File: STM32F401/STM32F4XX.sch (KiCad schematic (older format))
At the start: 34 parts, among them J1 DEBUG UART, J2 Conn_02x16_Counter_Clockwise, J3 USB_B_Mini, J4 Conn_02x16_Counter_Clockwise, J5 JTAG SWDIO SWCLK, SW1 ~RESET, U1 STM32F401RCT6, U2 LM1117-3.3, Y1 8MHz

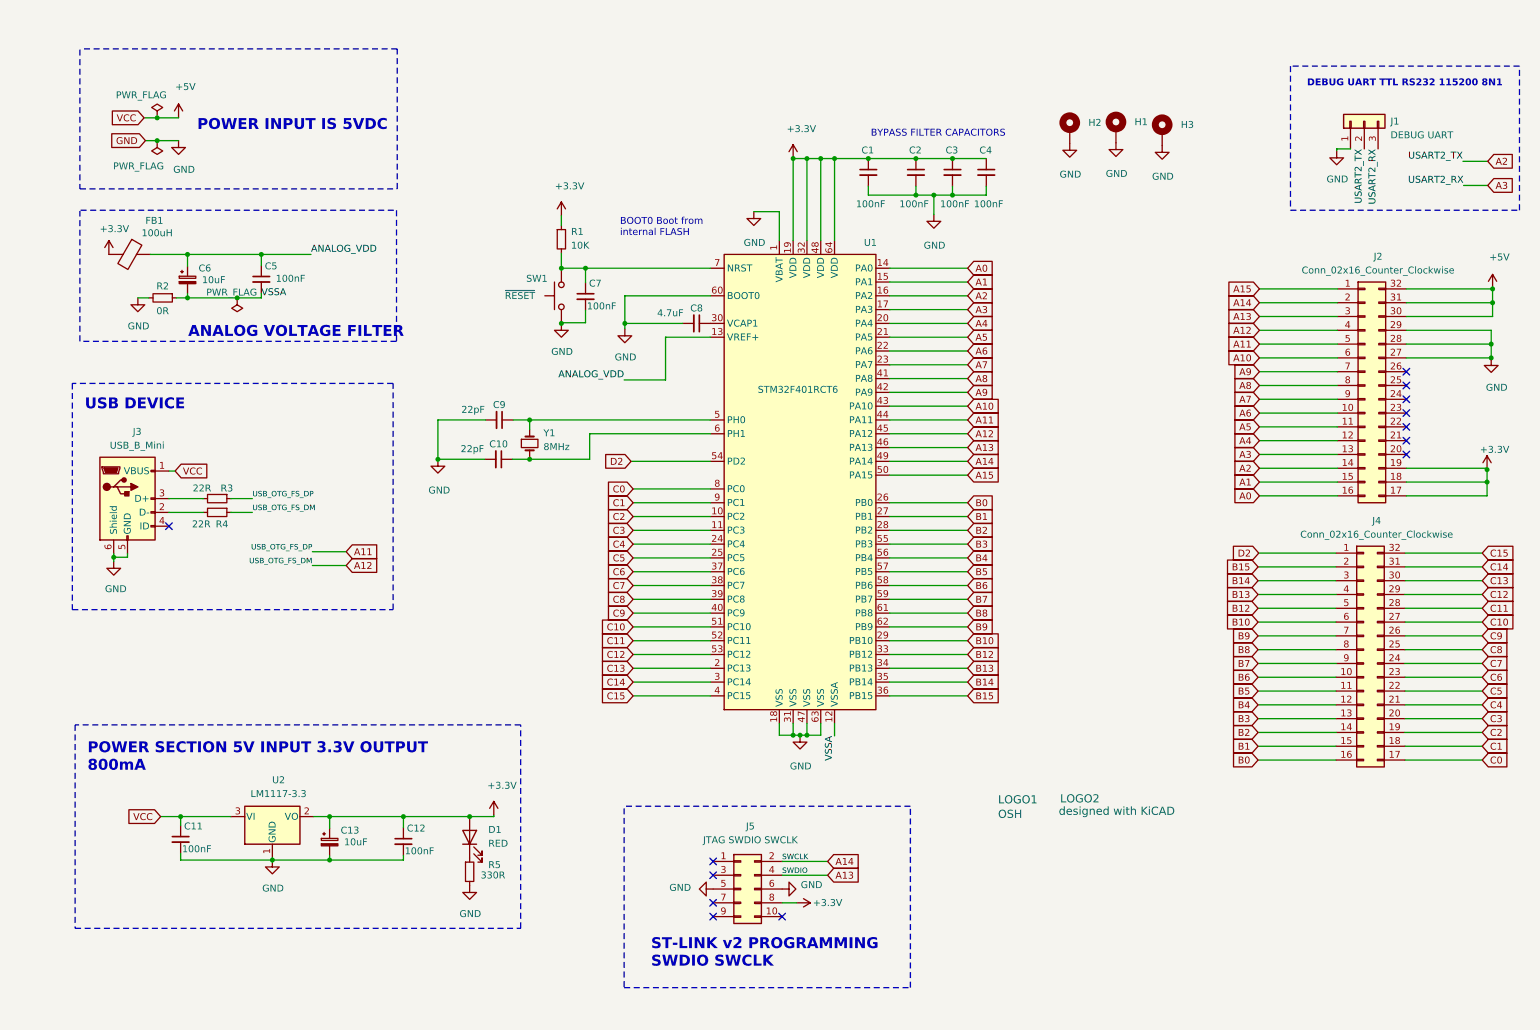
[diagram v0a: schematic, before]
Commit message: V0.4 USB+ and USB- bug, BOY UART
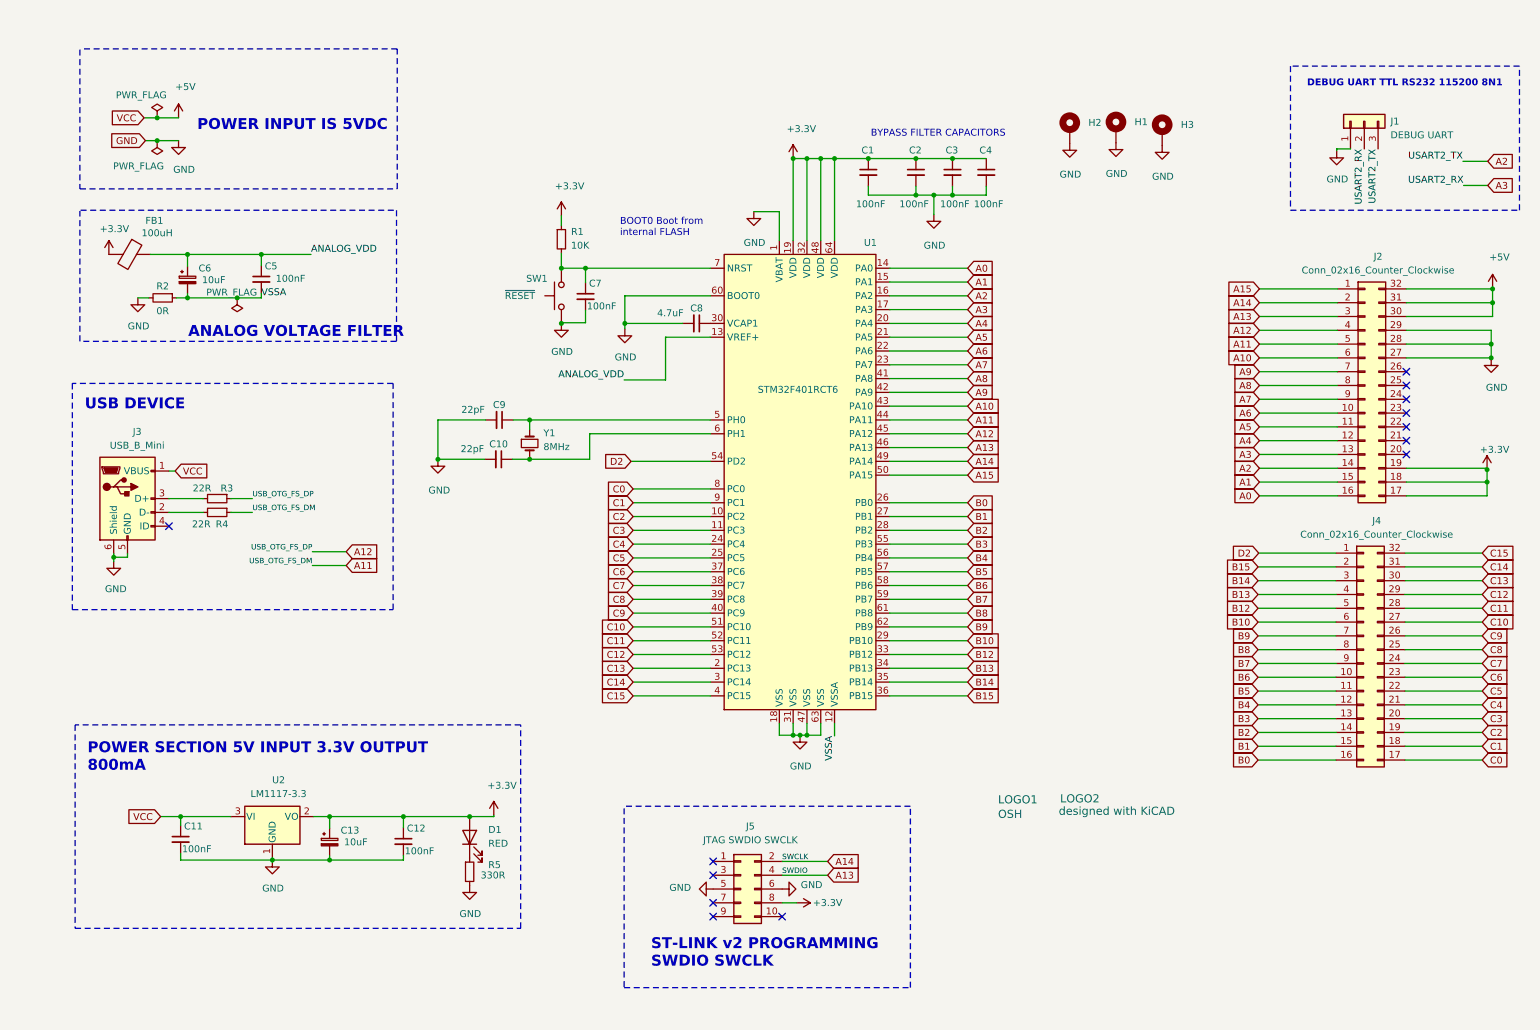
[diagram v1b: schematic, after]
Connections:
- net A11: now also R4.1; no longer R3.1
- net A12: now also R3.1; no longer R4.1
- net A2: now also J1.3 (Pin_3); no longer J1.2 (Pin_2)
- net A3: now also J1.2 (Pin_2); no longer J1.3 (Pin_3)
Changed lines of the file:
@@
 Sheet 1 1
 Title "GENERIC STM32F401 MODULE"
-Date "2022-02-08"
-Rev "0.3"
+Date "2023-02-15"
+Rev "0.4"
 Comp "RetroBit Lab"
 Comment1 ""
@@
 	1    0    0    -1
 $EndComp
+Text Label 10050 1290 3    50   ~ 0
+USART2_TX
 Text Label 9950 1290 3    50   ~ 0
-USART2_TX
-Text Label 10050 1290 3    50   ~ 0
 USART2_RX
 Wire Wire Line
@@
 A3
 Text GLabel 2570 4210 2    50   Input ~ 0
+A12
+Text GLabel 2570 4310 2    50   Input ~ 0
 A11
-Text GLabel 2570 4310 2    50   Input ~ 0
-A12
 Text Label 2325 4210 2    39   ~ 0
 USB_OTG_FS_DP

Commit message: Start transition to a smaller board. Using smallest components footprint
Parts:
- removed C1, C11, C12, C2, C3, C4, C5, C7: 100nF, Capacitor_SMD:C_1206_3216Metric_Pad1.33x1.80mm_HandSolder, symbol Device:C_Small
- removed C10, C9: 22pF, Capacitor_SMD:C_1206_3216Metric_Pad1.33x1.80mm_HandSolder, symbol Device:C_Small
- removed C13, C6: 10uF, Capacitor_Tantalum_SMD:CP_EIA-3216-12_Kemet-S_Pad1.58x1.35mm_HandSolder, symbol Device:CP_Small
- removed C8: 4.7uF, Capacitor_SMD:C_1206_3216Metric_Pad1.33x1.80mm_HandSolder, symbol Device:C_Small
- removed D1: RED, LED_SMD:LED_1206_3216Metric_Pad1.42x1.75mm_HandSolder, symbol Device:LED
- removed FB1: 100uH, Inductor_SMD:L_1206_3216Metric_Pad1.22x1.90mm_HandSolder, symbol Device:Ferrite_Bead
- removed J2, J4: Conn_02x16_Counter_Clockwise, Connector_PinHeader_2.54mm:PinHeader_2x16_P2.54mm_Vertical, symbol Connector_Generic:Conn_02x16_Counter_Clockwise
- removed J3: USB_B_Mini, Connector_USB:USB_Mini-B_Lumberg_2486_01_Horizontal, symbol Connector:USB_B_Mini
- removed J5: JTAG SWDIO SWCLK, Connector_IDC:IDC-Header_2x05_P2.54mm_Vertical, symbol Connector_Generic:Conn_02x05_Odd_Even
- removed R1: 10K, Resistor_SMD:R_1206_3216Metric_Pad1.30x1.75mm_HandSolder, symbol Device:R_Small
- removed R2: 0R, Resistor_SMD:R_1206_3216Metric_Pad1.30x1.75mm_HandSolder, symbol Device:R_Small
- removed R3, R4: 22R, Resistor_SMD:R_1206_3216Metric_Pad1.30x1.75mm_HandSolder, symbol Device:R_Small
- removed R5: 330R, Resistor_SMD:R_1206_3216Metric_Pad1.30x1.75mm_HandSolder, symbol Device:R_Small
- removed SW1: ~RESET, RetroBitLab:SPST-7.3x3.9x2.5-WUERTH-434121025816, symbol Switch:SW_Push
- removed U2: LM1117-3.3, Package_TO_SOT_SMD:SOT-223-3_TabPin2, symbol Regulator_Linear:LM1117-3.3
- removed Y1: 8MHz, Crystal:Crystal_SMD_HC49-SD, symbol Device:Crystal_Small
- added C1, C11, C12, C13, C2, C3, C4, C5, C7: 100nF, Capacitor_SMD:C_0603_1608Metric_Pad1.08x0.95mm_HandSolder, symbol CCAP0603:100nF
- added C10, C9: 22pF, Capacitor_SMD:C_0603_1608Metric_Pad1.08x0.95mm_HandSolder, symbol CCAP0603:22pF
- added C14, C6: 10uF, Capacitor_Tantalum_SMD:CP_EIA-3528-12_Kemet-T_Pad1.50x2.35mm_HandSolder, symbol TCAP3528:10uF-35V
- added C8: 4.7uF, Capacitor_SMD:C_0805_2012Metric_Pad1.18x1.45mm_HandSolder, symbol CCAP0805:4.7uF
- added J2, J4: CONN_02x16_PIN_SMD_Counter_Clockwise, Connector_PinHeader_2.54mm:PinHeader_2x16_P2.54mm_Vertical_SMD, symbol RetroBitLab:CONN_02x16_PIN_SMD_Counter_Clockwise
- added J3: DX07S016JA1R1500, RetroBitLab:JAE_DX07S016JA1R1500, symbol AmigaComponents:DX07S016JA1R1500
- added J5: CONN_SMD_HEADER_BOX_02x05_Odd_Even_2.54mm, RetroBitLab:IDC-Header_2x05_P2.54mm_Vertical_SMD, symbol AmigaComponents:CONN_SMD_HEADER_BOX_02x05_Odd_Even_2.54mm
- added L1: 90R@100MHZ, Inductor_SMD:L_0805_2012Metric_Pad1.15x1.40mm_HandSolder, symbol RetroBitLab:FB080590R100MHZ850mA
- added LD1: RED, LED_SMD:LED_1206_3216Metric_Pad1.42x1.75mm_HandSolder, symbol CLED1206:RED
- added R1: 10K, Resistor_SMD:R_0603_1608Metric_Pad0.98x0.95mm_HandSolder, symbol CRES0603:10K
- added R2: 0R, Resistor_SMD:R_0603_1608Metric_Pad0.98x0.95mm_HandSolder, symbol CRES0603:CREZ06031%
- added R3, R6: 5K1, Resistor_SMD:R_0603_1608Metric_Pad0.98x0.95mm_HandSolder, symbol CRES0603:5K1
- added R4, R5: 22R, Resistor_SMD:R_0603_1608Metric_Pad0.98x0.95mm_HandSolder, symbol CRES0603:22R
- added R7: 330R, Resistor_SMD:R_0603_1608Metric_Pad0.98x0.95mm_HandSolder, symbol CRES0603:330R
- added SW1: ~RESET, RetroBitLab:SPST-7.3x3.9x2.5-WUERTH-434121025816, symbol RetroBitLab:SPST2P
- added U2: AMS1117-3.3, Package_TO_SOT_SMD:SOT-223-3_TabPin2, symbol AmigaComponents:AMS1117-3.3
- added Y1: 8MHzC, Crystal:Crystal_SMD_HC49-SD_HandSoldering, symbol RetroBitLab:8MHzC
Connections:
- net labels added: DM, DP
- wire segments 221 -> 253
- no-connect marks 13 -> 14
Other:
- note added: "USB C / USB DEVICE"
- note removed: "USB DEVICE"
- moved on the sheet: H1, H2, H3, U1

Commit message: RetroBitLab library instead of AmigaComponents
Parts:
- J3: symbol AmigaComponents:DX07S016JA1R1500 -> RetroBitLab:DX07S016JA1R1500
- J5: symbol AmigaComponents:CONN_SMD_HEADER_BOX_02x05_Odd_Even_2.54mm -> RetroBitLab:CONN_SMD_HEADER_BOX_02x05_Odd_Even_2.54mm
- LOGO1, LOGO2: symbol AmigaComponents:LOGO -> RetroBitLab:LOGO
- U2: symbol AmigaComponents:AMS1117-3.3 -> RetroBitLab:AMS1117-3.3
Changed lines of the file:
@@
 	7455 1545 7455 1685
 $Comp
-L AmigaComponents:LOGO LOGO1
+L RetroBitLab:LOGO LOGO1
 U 1 1 61DE4C48
 P 7270 6060
@@
 $EndComp
 $Comp
-L AmigaComponents:LOGO LOGO2
+L RetroBitLab:LOGO LOGO2
 U 1 1 62003E98
 P 7705 6105
@@
 $EndComp
 $Comp
-L AmigaComponents:DX07S016JA1R1500 J3
+L RetroBitLab:DX07S016JA1R1500 J3
 U 1 1 6905C807
 P 1660 4490
@@
 	6060 6455 5730 6455
 $Comp
-L AmigaComponents:CONN_SMD_HEADER_BOX_02x05_Odd_Even_2.54mm J5
+L RetroBitLab:CONN_SMD_HEADER_BOX_02x05_Odd_Even_2.54mm J5
 U 1 1 6907C8E5
 P 5430 6755
@@
 	3835 7110 3835 7140
 $Comp
-L AmigaComponents:AMS1117-3.3 U2
+L RetroBitLab:AMS1117-3.3 U2
 U 1 1 69067808
 P 2405 6690

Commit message: V2.0 Smaller
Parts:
- removed J2, J4: CONN_02x16_PIN_SMD_Counter_Clockwise, Connector_PinHeader_2.54mm:PinHeader_2x16_P2.54mm_Vertical_SMD, symbol RetroBitLab:CONN_02x16_PIN_SMD_Counter_Clockwise
- added H4: MountingHole_Pad, MountingHole:MountingHole_3.2mm_M3_DIN965_Pad, symbol Mechanical:MountingHole_Pad
- added J2, J4: CONN_02x16_PIN_SMD_Odd_Even_2.54mm, Connector_PinHeader_2.54mm:PinHeader_2x16_P2.54mm_Vertical_SMD, symbol RetroBitLab:CONN_02x16_PIN_SMD_Odd_Even_2.54mm
- added JP1: ~BOOTLOADER, Connector_PinHeader_2.54mm:PinHeader_1x02_P2.54mm_Vertical, symbol Connector_Generic:Conn_01x02
- added LD2: GREEN, LED_SMD:LED_0805_2012Metric_Pad1.15x1.40mm_HandSolder, symbol CLED0805:GREEN
- added R8: 470R, Resistor_SMD:R_0603_1608Metric_Pad0.98x0.95mm_HandSolder, symbol CRES0603:470R
- added R9: 0R, Resistor_SMD:R_0603_1608Metric_Pad0.98x0.95mm_HandSolder, symbol CRES0603:CREZ06031%
- Y1: footprint Crystal:Crystal_SMD_HC49-SD_HandSoldering -> Crystal:Crystal_SMD_HC49-SD
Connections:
- wire segments 253 -> 284
- no-connect marks 14 -> 8
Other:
- note added: "ACTIVITY LED\nCan be disabled"
- note added: "CLOSE TO FORCE BOOTLOADER MODE"
